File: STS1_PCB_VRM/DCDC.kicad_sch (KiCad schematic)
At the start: 24 parts

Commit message: more work done
All parts besides RF added
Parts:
- C36, C47: value ~ -> 100uF; footprint (none) -> Capacitor_Tantalum_SMD:CP_EIA-7343-43_Kemet-X
- C37: value ~ -> 22uF; footprint (none) -> Capacitor_SMD:C_1206_3216Metric
- C38, C42, C43, C44: value ~ -> 100nF; footprint (none) -> Capacitor_SMD:C_0603_1608Metric
- C39, C40: value ~ -> 1uF; footprint (none) -> Capacitor_SMD:C_0805_2012Metric
- C41: value ~ -> 22nF; footprint (none) -> Capacitor_SMD:C_0603_1608Metric
- C45, C46: value ~ -> 10uF; footprint (none) -> Capacitor_SMD:C_0805_2012Metric
- D10: value ~ -> BZY55C12 RYG; footprint (none) -> Diode_SMD:D_0805_2012Metric
- D11: value ~ -> AQ1003-01LTG; footprint (none) -> Diode_SMD:D_SOD-523
- D9: value ~ -> UCLAMP0871P.TNT; footprint (none) -> STS_Package_DFN_QFN:SGP1610N2
- L2: value ~ -> 4.7uH; footprint (none) -> Inductor_SMD:L_12x12mm_H6mm
- Q2: value ~ -> BSS123; footprint (none) -> Package_TO_SOT_SMD:SOT-23
- R14: value ~ -> 10k; footprint (none) -> Resistor_SMD:R_0603_1608Metric
- R15: value ~ -> 1M; footprint (none) -> Resistor_SMD:R_0603_1608Metric
- R16: value ~ -> 100mR; footprint (none) -> Resistor_SMD:R_0603_1608Metric
- R17: value ~ -> 100k; footprint (none) -> Resistor_SMD:R_0603_1608Metric
- R18: value ~ -> 33k; footprint (none) -> Resistor_SMD:R_0603_1608Metric
- R19: value ~ -> 21k5; footprint (none) -> Resistor_SMD:R_0603_1608Metric
- U6: footprint (none) -> STS_Package_DFN_QFN:MP28167_QFN16

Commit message: V2.5
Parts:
- removed D10: BZY55C12 RYG, Diode_SMD:D_0805_2012Metric, symbol Device:D_Zener
- removed D11: AQ1003-01LTG, Diode_SMD:D_SOD-523, symbol Device:D_Zener
- removed D9: UCLAMP0871P.TNT, STS_Package_DFN_QFN:SGP1610N2, symbol Device:D_Zener
- removed U6: ~, STS_Package_DFN_QFN:MP28167_QFN16, symbol STS1_DCDC:MP28167GQ
- added C79: 100nF, symbol Device:C
- added D1: UCLAMP0871P.TNT, STS_Package_DFN_QFN:SGP1610N2, symbol Device:D_Zener
- added D3: BZY55C12 RYG, Diode_SMD:D_0805_2012Metric, symbol Device:D_Zener
- added D4: AQ1003-01LTG, Diode_SMD:D_SOD-523, symbol Device:D_Zener
- added U6: MP28167GQ, STS_Package_DFN_QFN:MP28167_QFN16, symbol STS_Regulator_Switching:MP28167GQ
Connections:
- net AGND: now also C79.2, D1.2 (A), D3.2 (A), D4.2 (A), U6.10 (AGND), U6.11 (GND), U6.2 (GND), U6.4 (NC), U6.5 (RSV1), U6.6 (RSV2), U6.8 (NC)
- net VIN: now also D1.1 (K), U6.1 (IN)
- net VOUT: now also D4.1 (K), U6.12 (OUT)
- net at C41.1, R19.1: now also U6.7 (OC)
- net at Q2.1 (G), R14.1, R15.1: now also D3.1 (K)
- net at Q2.3 (D), R17.2, R18.1: now also C79.1, U6.3 (EN)
- net at C40.1: now also U6.9 (VCC)
- net at C42.1, L2.1: now also U6.15 (SW1)
- net at C43.1, L2.2: now also U6.14 (SW2)
- net at C43.2: now also U6.13 (BST2)
- net at C42.2: now also U6.16 (BST1)
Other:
- note added: "DNP"

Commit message: Set all passive components (except in the RF path) to 0603
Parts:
- C37: footprint Capacitor_SMD:C_1206_3216Metric -> Capacitor_SMD:C_0603_1608Metric
- C39, C40, C45, C46: footprint Capacitor_SMD:C_0805_2012Metric -> Capacitor_SMD:C_0603_1608Metric
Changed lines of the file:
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@@
       (effects (font (size 1.27 1.27)) (justify left))
     )
-    (property "Footprint" "Capacitor_SMD:C_0805_2012Metric" (id 2) (at 215.5952 90.805 0)
+    (property "Footprint" "Capacitor_SMD:C_0603_1608Metric" (id 2) (at 215.5952 90.805 0)
       (effects (font (size 1.27 1.27)) hide)
     )
@@
       (effects (font (size 1.27 1.27)) (justify left))
     )
-    (property "Footprint" "Capacitor_SMD:C_0805_2012Metric" (id 2) (at 204.1652 90.805 0)
+    (property "Footprint" "Capacitor_SMD:C_0603_1608Metric" (id 2) (at 204.1652 90.805 0)
       (effects (font (size 1.27 1.27)) hide)
     )
@@
       (effects (font (size 1.27 1.27)) (justify left))
     )
-    (property "Footprint" "Capacitor_SMD:C_0805_2012Metric" (id 2) (at 93.6752 76.835 0)
+    (property "Footprint" "Capacitor_SMD:C_0603_1608Metric" (id 2) (at 93.6752 76.835 0)
       (effects (font (size 1.27 1.27)) hide)
     )
@@
       (effects (font (size 1.27 1.27)) (justify left))
     )
-    (property "Footprint" "Capacitor_SMD:C_1206_3216Metric" (id 2) (at 69.5452 69.215 0)
+    (property "Footprint" "Capacitor_SMD:C_0603_1608Metric" (id 2) (at 69.5452 69.215 0)
       (effects (font (size 1.27 1.27)) hide)
     )
@@
       (effects (font (size 1.27 1.27)) (justify left))
     )
-    (property "Footprint" "Capacitor_SMD:C_0805_2012Metric" (id 2) (at 126.0602 83.185 0)
-      (effects (font (size 1.27 1.27)) hide)
-    )
+    (property "Footprint" "Capacitor_SMD:C_0603_1608Metric" (id 2) (at 126.0602 83.185 0)
+      (effects (font (size 1.27 1.27)) hide)
+    )

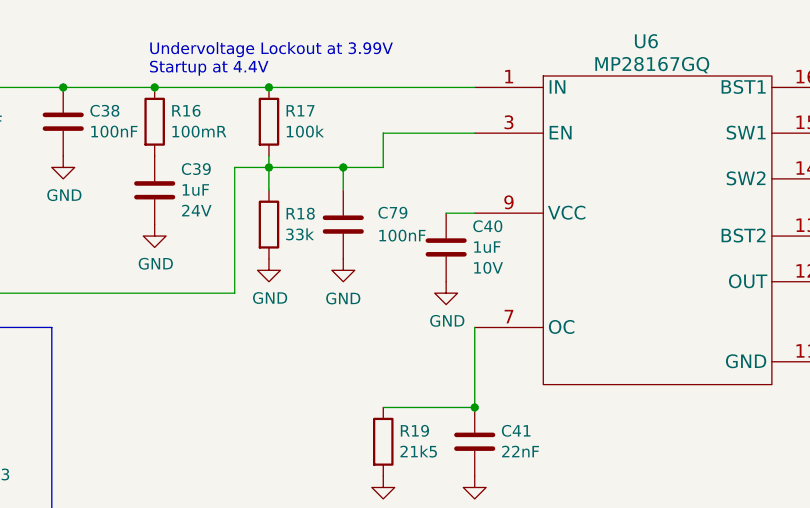
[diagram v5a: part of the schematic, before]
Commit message: Add missing C79 capacitor
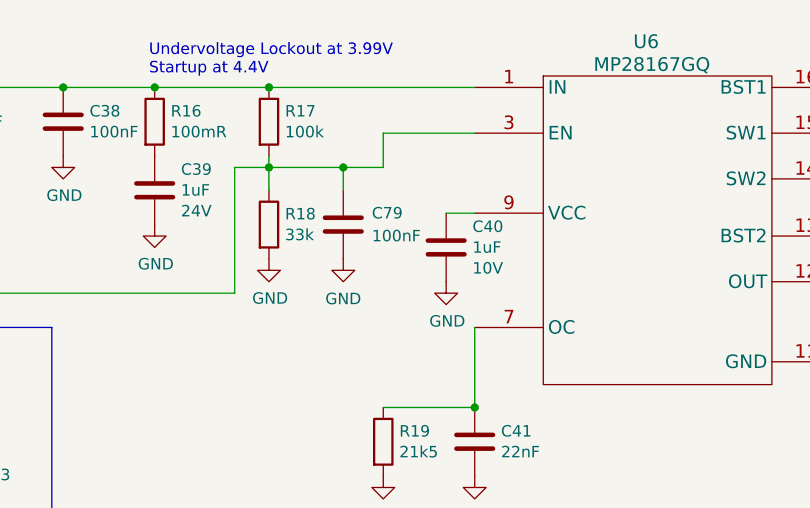
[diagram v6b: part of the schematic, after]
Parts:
- C79: footprint (none) -> Capacitor_SMD:C_0603_1608Metric
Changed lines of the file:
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@@
   (symbol (lib_id "Device:C") (at 113.665 76.835 0) (unit 1)
     (in_bom yes) (on_board yes) (fields_autoplaced)
-    (property "Reference" "C79" (id 0) (at 117.475 75.5649 0)
+    (property "Reference" "C79" (id 0) (at 116.84 75.5649 0)
       (effects (font (size 1.27 1.27)) (justify left))
     )
-    (property "Value" "100nF" (id 1) (at 117.475 78.1049 0)
+    (property "Value" "100nF" (id 1) (at 116.84 78.1049 0)
       (effects (font (size 1.27 1.27)) (justify left))
     )
-    (property "Footprint" "" (id 2) (at 114.6302 80.645 0)
+    (property "Footprint" "Capacitor_SMD:C_0603_1608Metric" (id 2) (at 114.6302 80.645 0)
       (effects (font (size 1.27 1.27)) hide)
     )

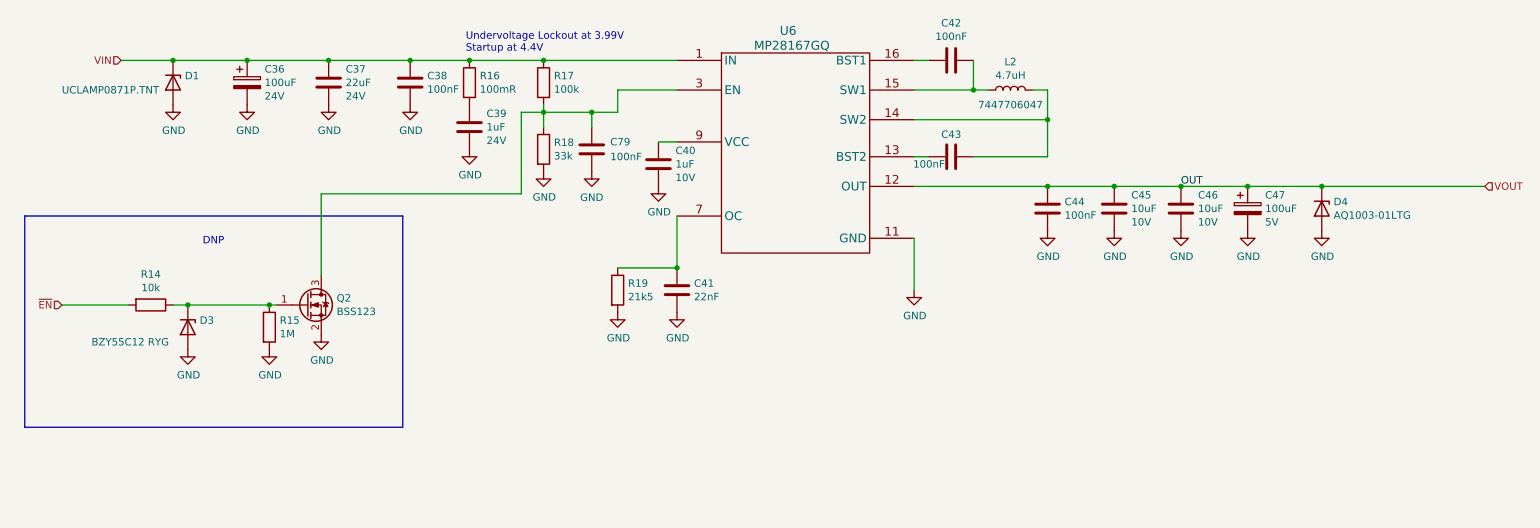
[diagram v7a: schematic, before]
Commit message: feat: update RF hardware and clean up ERC errors
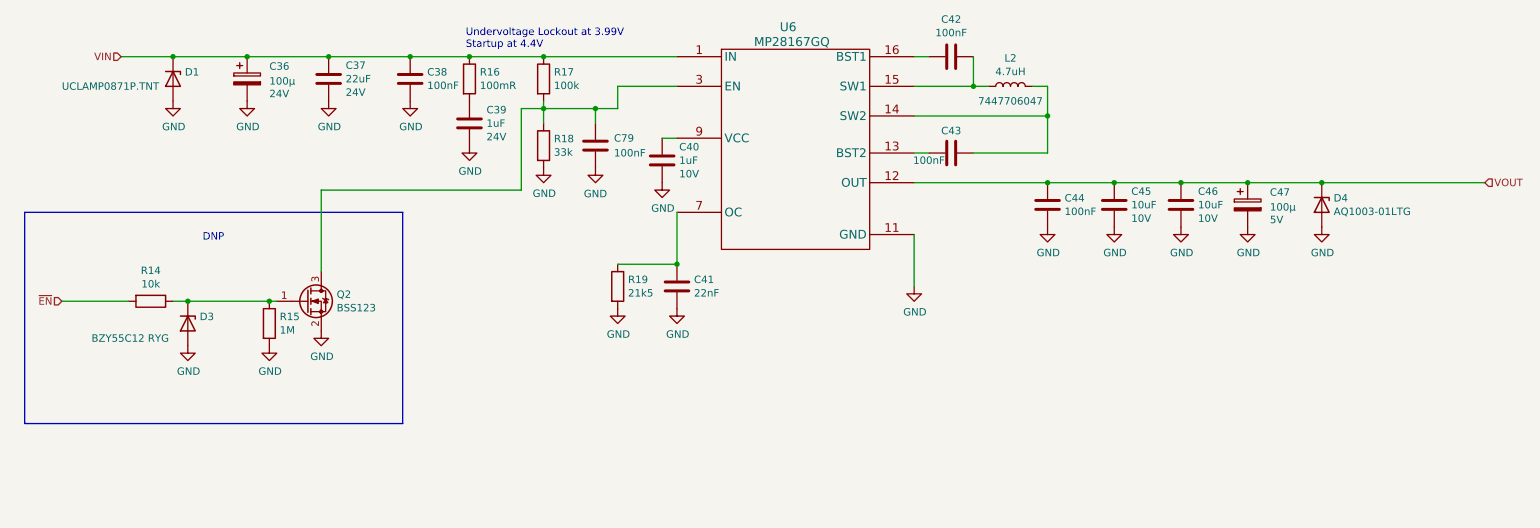
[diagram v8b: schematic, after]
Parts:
- removed C36, C47: 100uF, Capacitor_Tantalum_SMD:CP_EIA-7343-43_Kemet-X, symbol STS1_VRM-rescue:CP-Device
- added C36, C47: 100µ, Capacitor_Tantalum_SMD:CP_EIA-7343-43_Kemet-X, symbol Device:C_Polarized
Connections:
- net AGND: now also C36.2, C47.2
- net VIN: now also C36.1
- net VOUT: now also C47.1
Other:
- moved on the sheet: C37, C38, C39, C40, C41, C42, C43, C44, C45, C46, C79, D1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
